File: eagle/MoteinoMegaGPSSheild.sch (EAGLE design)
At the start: 30 parts, among them J1 BilgeSwitch, J2 Button, J3 LED, J4 DS18B20, J5 DS18B20, J6 GND, J7 OKI-78SR-5/1.5, J8 5V, J9 12-24V_VCC, Q1 NDP6020P, Q2 IRF9Z14PBF, Q3 2N7000, Q4 IRF9Z14PBF, Q5 2N7000

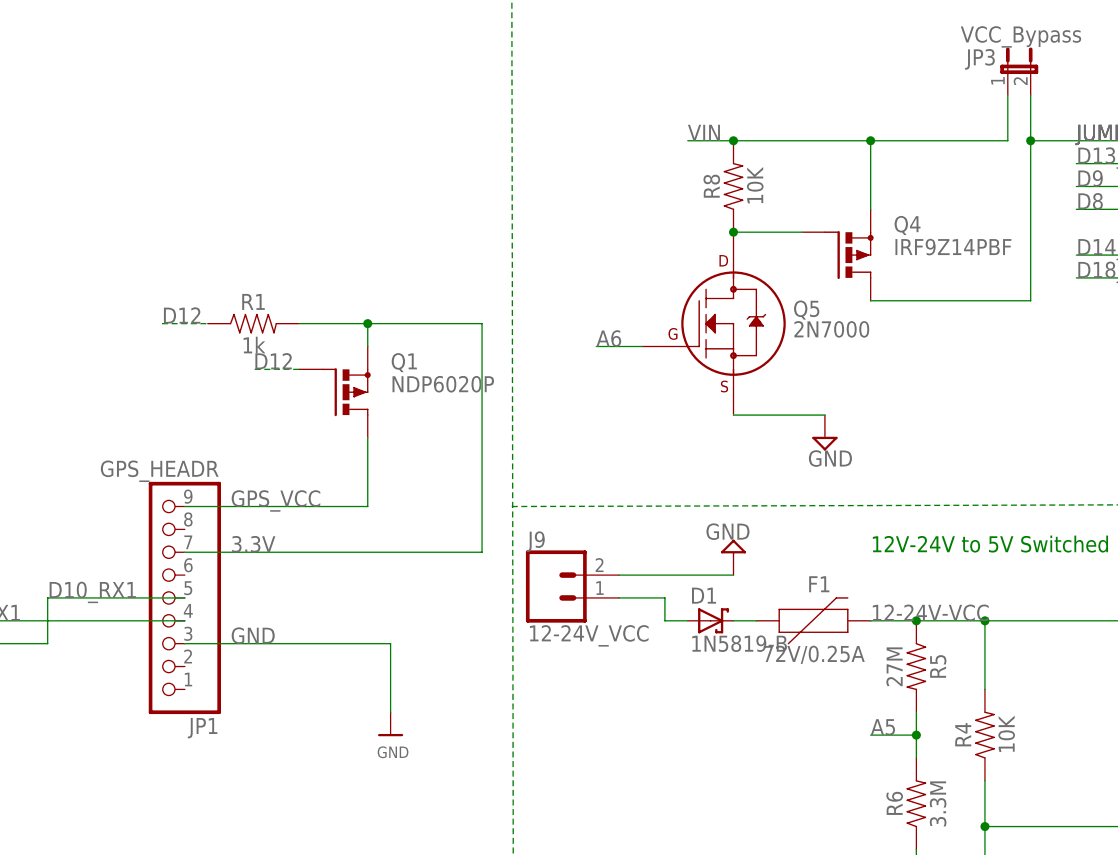
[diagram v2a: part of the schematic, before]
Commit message: Changed Resistor shapes
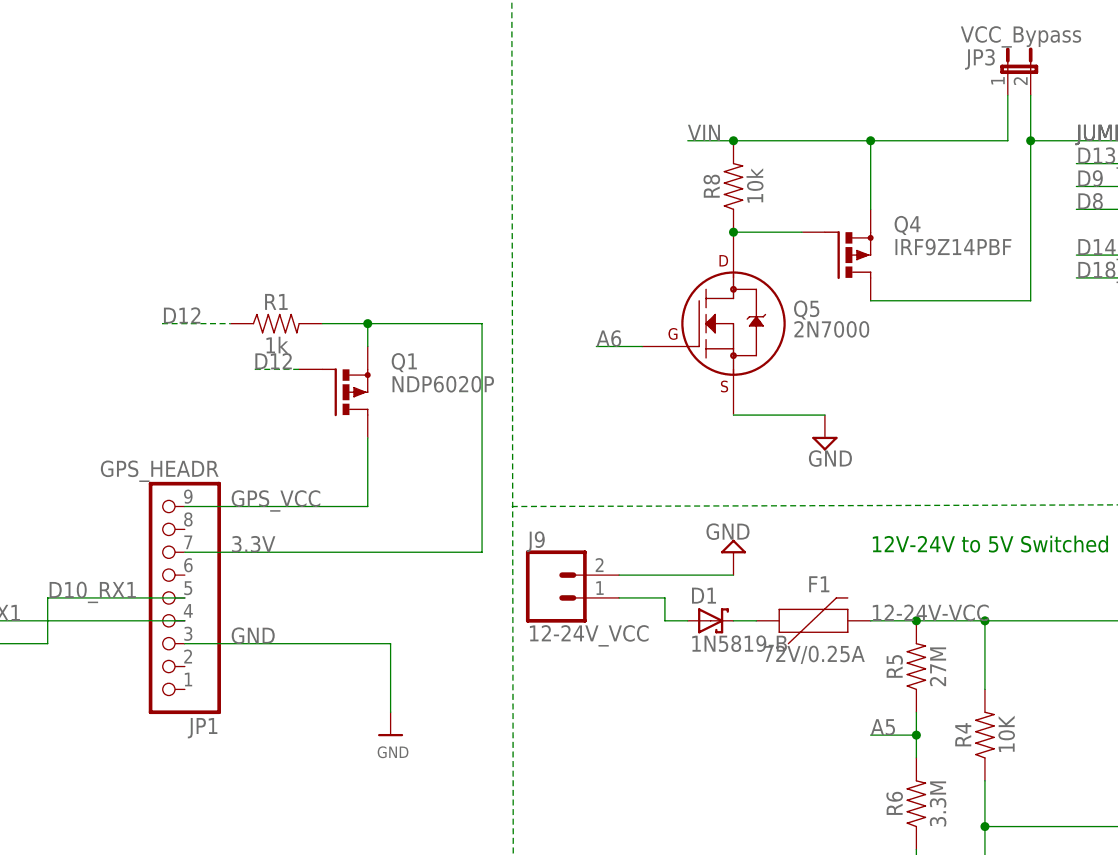
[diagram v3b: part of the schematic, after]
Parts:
- R2, R3, R4, R5, R6, R7: device SparkFun-Resistors:1MOHM-HORIZ_KIT-1/6W-5% -> SparkFun-Resistors:1KOHM-HORIZ-1/4W-1%
- R8: value 10K -> 10k; device SparkFun-Resistors:1MOHM-HORIZ_KIT-1/6W-5% -> SparkFun-Resistors:1KOHM-HORIZ-1/4W-1%
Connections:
- net 12-24V-VCC: now also R5.2; no longer R5.1
- net A5: now also R5.1; no longer R5.2
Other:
- moved on the sheet: R1, R5

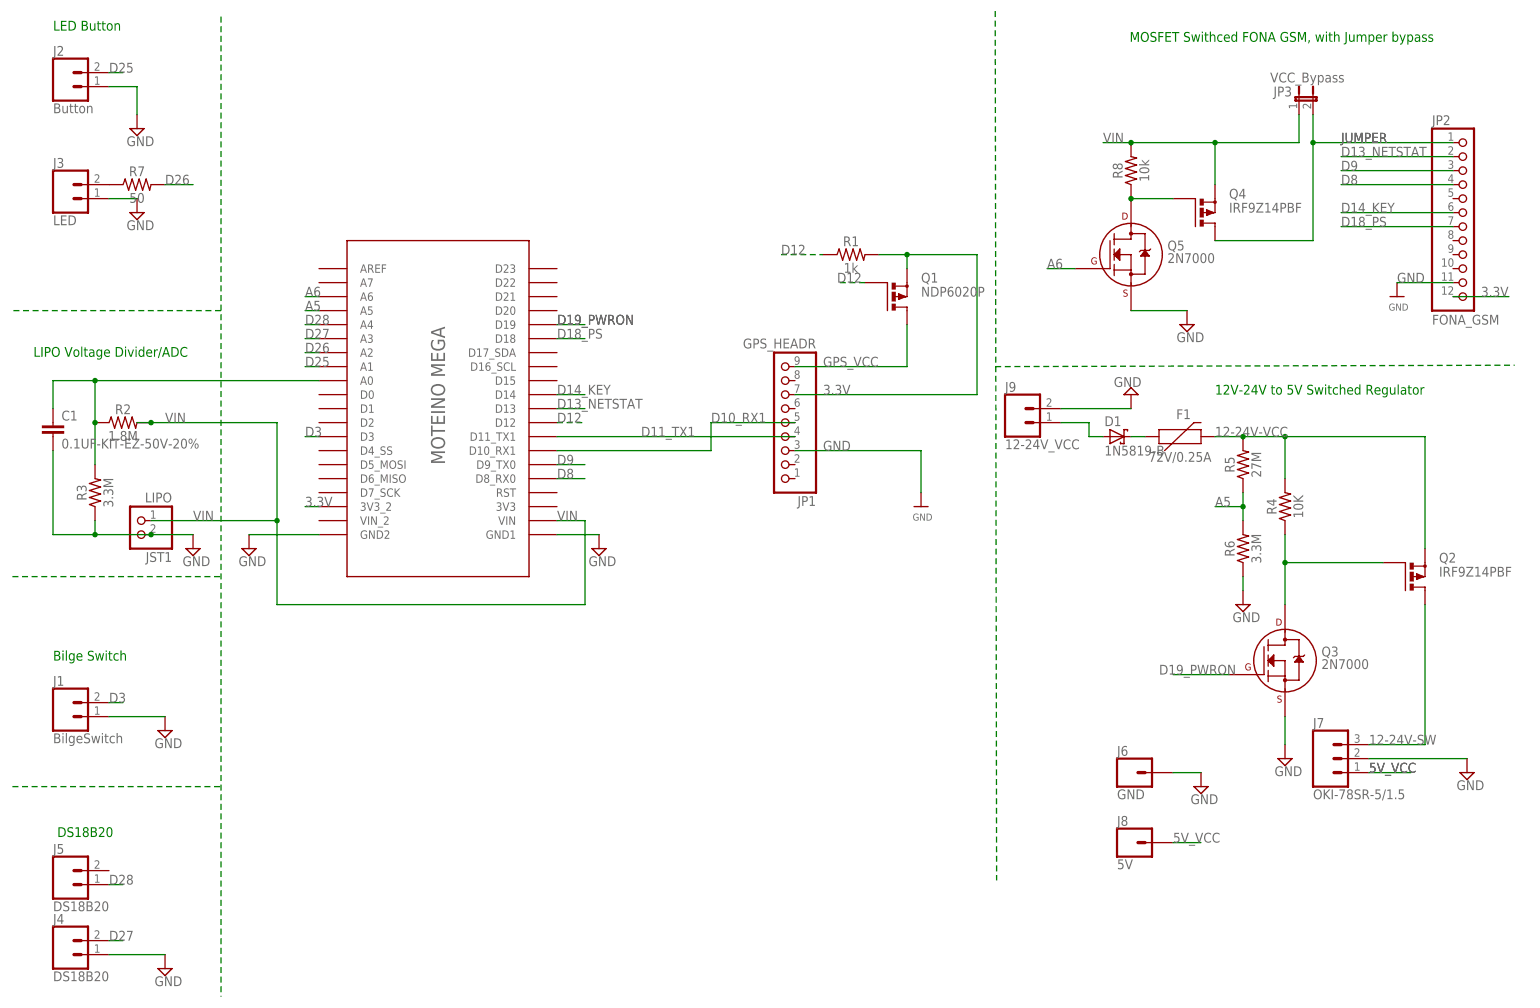
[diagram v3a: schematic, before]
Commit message: Added current limiting resistors
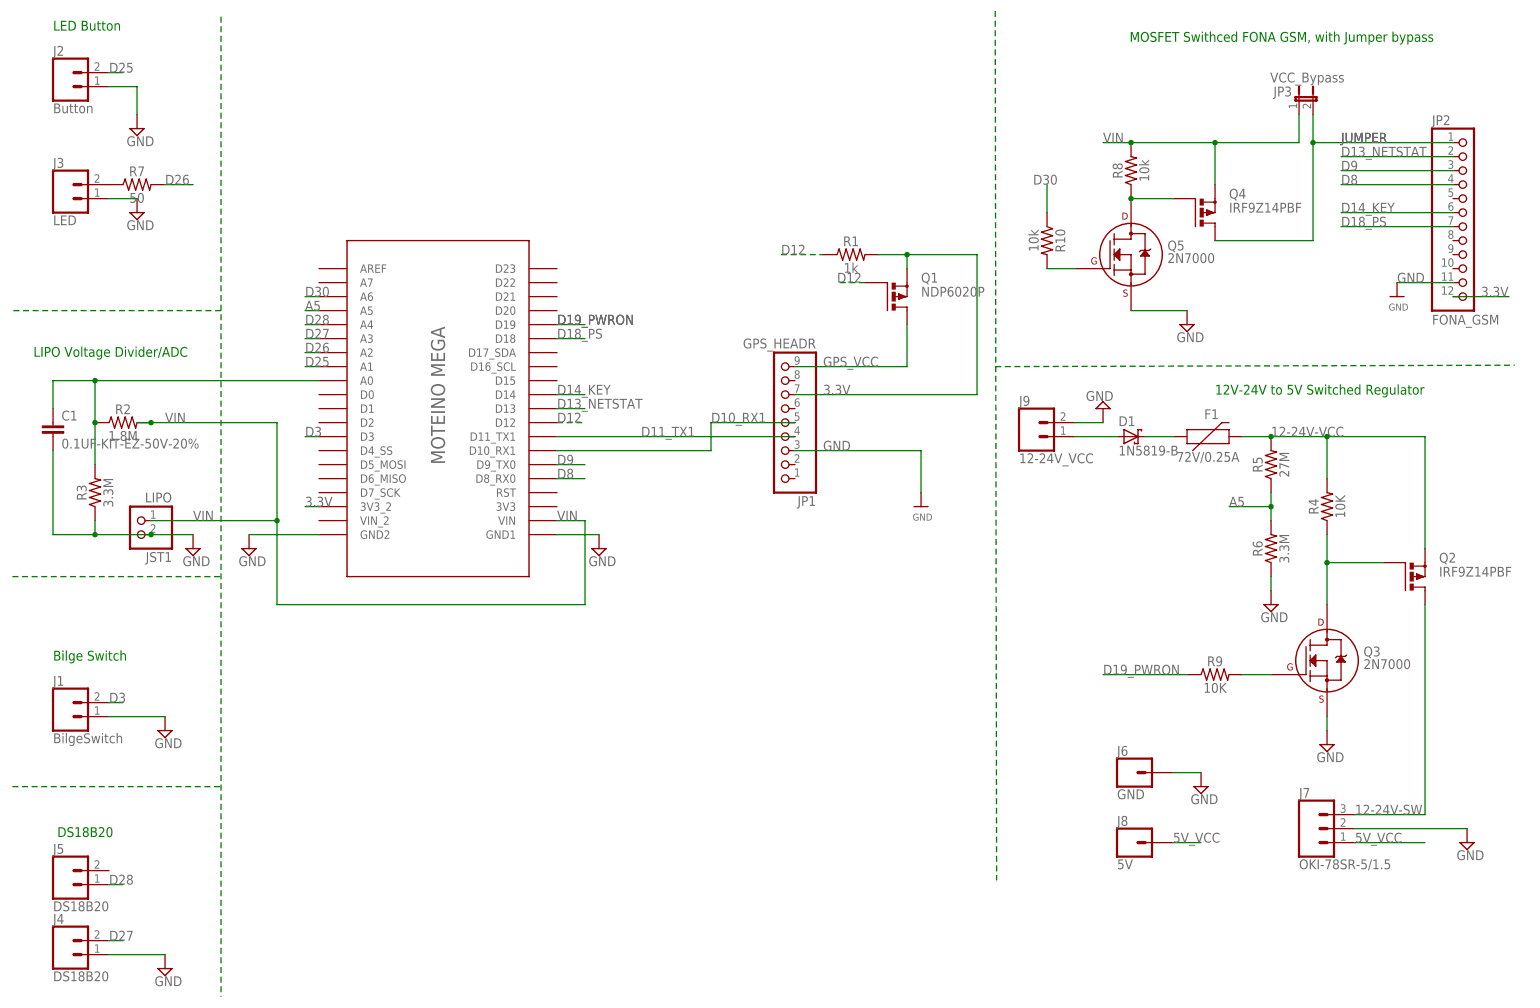
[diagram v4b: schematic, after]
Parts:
- added R10: 10k, SparkFun-Resistors:1KOHM-HORIZ-1/4W-1%
- added R9: 10K, SparkFun-Resistors:1KOHM-HORIZ-1/4W-1%
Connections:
- removed net A6: MOTEINO_MEGA.A6, Q5.G
- new net D30: MOTEINO_MEGA.A6, R10.1
- new net N$10: Q5.G, R10.2
- new net N$9: Q3.G, R9.2
- net D19_PWRON: now also R9.1; no longer Q3.G
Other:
- moved on the sheet: D1, F1, J7, J9, Q3, R4, R5, R6

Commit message: Routed 100%, finally
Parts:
- JP2: value FONA_GSM -> FONA GSM
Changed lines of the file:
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@@
 <part name="SUPPLY4" library="supply2" deviceset="GND" device=""/>
 <part name="U$31" library="microbuilder" deviceset="GND" device=""/>
-<part name="JP2" library="adafruit2" deviceset="PINHD-1X12" device="-CB" value="FONA_GSM"/>
+<part name="JP2" library="adafruit2" deviceset="PINHD-1X12" device="-CB" value="FONA GSM"/>
 <part name="SUPPLY5" library="supply2" deviceset="GND" device=""/>
 <part name="J2" library="SparkFun-Connectors" deviceset="CONN_02" device="3.5MM-NO_SILK" value="Button"/>

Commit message: eagle updates
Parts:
- removed D1: 1N5819-B, diode:1N5819-B
- removed F1: 72V/0.25A, SparkFun-Fuses:PPTC_PTH
- removed J1: BilgeSwitch, SparkFun-Connectors:CONN_023.5MM-NO_SILK
- removed J2: Button, SparkFun-Connectors:CONN_023.5MM-NO_SILK
- removed J3: LED, SparkFun-Connectors:CONN_023.5MM-NO_SILK
- removed J4, J5: DS18B20, SparkFun-Connectors:CONN_023.5MM-NO_SILK
- removed J6: GND, SparkFun-Connectors:CONN_01
- removed J7: OKI-78SR-5/1.5, SparkFun-Connectors:CONN_03
- removed J8: 5V, SparkFun-Connectors:CONN_01
- removed J9: 12-24V_VCC, SparkFun-Connectors:CONN_023.5MM-NO_SILK
- removed JP2: FONA GSM, adafruit2:PINHD-1X12-CB
- removed JP3: VCC_Bypass, jumper:JP1E
- removed Q1: NDP6020P, transistor-power:PMOSFET_PTO220BV
- removed Q3, Q5: 2N7000, transistors:2N7002_TO92
- removed Q4: IRF9Z14PBF, transistor-power:PMOSFET_PTO220BV
- removed R1: 1k, SparkFun-Resistors:1KOHM-HORIZ-1/4W-1%
- removed R10, R8: 10k, SparkFun-Resistors:1KOHM-HORIZ-1/4W-1%
- removed R4, R9: 10K, SparkFun-Resistors:1KOHM-HORIZ-1/4W-1%
- added 5V: 5V, SparkFun-Connectors:CONN_02
- added C2: 0.1U, SparkFun-Capacitors:0.1UF-KIT-EZ-50V-20%
- added FONA: (no value), SparkFun-Connectors:CONN_12
- added GND, GND_II: GND, SparkFun-Connectors:CONN_02
- added IO: (no value), SparkFun-Connectors:CONN_09
- added JST_PWR: VVC_5V, SparkFun-Connectors:CONN_04JST-PTH
- added VCC: VCC, SparkFun-Connectors:CONN_02
- C1: value 0.1UF-KIT-EZ-50V-20% -> 0.1U
- Q2: value IRF9Z14PBF -> 60V/32A/35mΩ; device transistor-power:PMOSFET_PTO220BV -> SparkFun-DiscreteSemi:MOSFET-NCH-FQP30N06L
- R5: value 27M -> 3.3M
- R6: value 3.3M -> 27M; device SparkFun-Resistors:1KOHM-HORIZ-1/4W-1% -> adafruit:R-US_0309/12
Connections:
- net D10_RX1 renamed D10_GPS_RX
- net D11_TX1 renamed D11_GPS_TX
- net D26 renamed D26_LED
- removed net 12-24V-SW: J7.3, Q2.D
- removed net 12-24V-VCC: F1.2, Q2.S, R4.2, R5.2
- removed net 5V_VCC: J7.1, J8.1
- removed net A5: MOTEINO_MEGA.A5, R5.1, R6.2
- removed net D12: MOTEINO_MEGA.D12, Q1.G, R1.1
- removed net D13_NETSTAT: JP2.2, MOTEINO_MEGA.D13
- removed net D14_KEY: JP2.6, MOTEINO_MEGA.D14
- removed net D18_PS: JP2.7, MOTEINO_MEGA.D18
- removed net D25: J2.2, MOTEINO_MEGA.A1
- removed net D27: J4.2, MOTEINO_MEGA.A3
- removed net D28: J5.1, MOTEINO_MEGA.A4
- removed net D3: J1.2, MOTEINO_MEGA.D3
- removed net D30: MOTEINO_MEGA.A6, R10.1
- removed net D8: JP2.4, MOTEINO_MEGA.D8_RX0
- removed net D9: JP2.3, MOTEINO_MEGA.D9_TX0
- removed net GPS_VCC: JP1.9, Q1.D
- removed net JUMPER: JP2.1, JP3.2, Q4.D
- removed net N$10: Q5.G, R10.2
- removed net N$5: Q4.G, Q5.D, R8.1
- removed net N$6: D1.A, J9.1
- removed net N$7: J3.2, R7.1
- removed net N$8: D1.C, F1.1
- removed net N$9: Q3.G, R9.2
- removed net SPEAKER2+: JP2.10
- new net 5V: 5V.1, 5V.2, JST_PWR.2
- new net A5_VCC_VD: C2.1, MOTEINO_MEGA.A5, R5.2, R6.1
- new net D12_GPS_MOS_N: MOTEINO_MEGA.D12, Q2.G
- new net D13_FONA_NETSTAT: FONA.2, MOTEINO_MEGA.D13
- new net D14_FONA_KEY: FONA.6, MOTEINO_MEGA.D14
- new net D18_FONA_PS: FONA.7, MOTEINO_MEGA.D18
- new net D25_LED_SWITCH: IO.9, MOTEINO_MEGA.A1
- new net D27_DS_PWR: IO.2, MOTEINO_MEGA.A3
- new net D28_DS_DATA: IO.3, MOTEINO_MEGA.A4
- new net D3_BILGESW: IO.5, MOTEINO_MEGA.D3
- new net D8_FONA_TX: FONA.3, MOTEINO_MEGA.D8_RX0
- new net D9_FONA_RX: FONA.4, MOTEINO_MEGA.D9_TX0
- new net N$1: JP1.3, Q2.D
- new net VCC: JST_PWR.4, R6.2, VCC.2
- net 3.3V: now also FONA.1, MOTEINO_MEGA.RST; no longer JP2.12, Q1.S, R1.2
- net D19_PWRON: now also VCC.1; no longer R9.1
- net GND: now also C2.2, FONA.11, GND.1, GND.2, GND_II.1, GND_II.2, IO.1, IO.4, IO.6, IO.8, JST_PWR.1, JST_PWR.3, Q2.S, R5.1; no longer J1.1, J2.1, J3.1, J4.1, J6.1, J7.2, J9.2, JP1.3, JP2.11, Q3.S, Q5.S, R6.1
- net N$2: now also IO.7, R7.1; no longer Q2.G, Q3.D, R4.1
- net VIN: now also FONA.12, MOTEINO_MEGA.VIN_2; no longer JP3.1, Q4.S, R8.2
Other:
- note added: "Mini Step Down Voltage Reg Buck Module 4.5v~55V VCC 5V Output Max 600mA, 96% eff"
- note added: "VCC Voltage Divider/ADC"
- note removed: "12V-24V to 5V Switched Regulator"
- note removed: "Bilge Switch"
- note removed: "DS18B20"
- note removed: "LED Button"
- note removed: "MOSFET Swithced FONA GSM, with Jumper bypass"
- moved on the sheet: C1, JP1, JST1, R2, R3, R5, R6, R7
